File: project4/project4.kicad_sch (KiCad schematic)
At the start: 22 parts, among them J1 Conn_02x07_Row_Letter_First, J2 Conn_02x07_Row_Letter_First, U1 SST27ST020, U2 SST27ST020, U3 74LS02, U4 74LS670, U5 74LS139, U6 74LS670

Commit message: Modify project4
Signed-off-by: Youngki Park <ykp7409@gmail.com>
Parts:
- removed U3: 74LS02, Package_DIP:DIP-14_W7.62mm_Socket, symbol 74xx:74LS02
- added U7: 74LS32, symbol 74xx:74LS32
- added U8: 74LS00, symbol 74xx:74LS00
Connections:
- net +5V: now also U7.14 (VCC)
- net A13: now also U8.1
- net A15: now also U7.9
- net D0: now also U4.15 (D1); no longer U4.3 (D4)
- net D1: now also U4.1 (D2); no longer U4.2 (D3)
- net D2: now also U4.2 (D3); no longer U4.1 (D2)
- net D3: now also U4.3 (D4); no longer U4.15 (D1)
- net GND: now also U4.11 (~{Er}), U6.11 (~{Er}), U7.7 (GND)
- net MA13: now also R4.2, U4.10 (Q1); no longer R1.2, U4.6 (Q4)
- net MA14: now also R3.2, U4.9 (Q2); no longer R2.2, U4.7 (Q3)
- net MA15: now also R2.2, U4.7 (Q3); no longer R3.2, U4.9 (Q2)
- net MA16: now also R1.2, U4.6 (Q4); no longer R4.2, U4.10 (Q1)
- net /SLTSL: now also U7.2
- net /WR: now also U7.1
- net at U4.12 (~{Ew}), U6.12 (~{Ew}): now also U7.6
- new net: U7.10, U8.3
- new net: U7.4, U7.8
- new net: U7.3, U7.5
- new net A14: U8.2
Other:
- moved on the sheet: C3, C5, J1, J2, R1, R2, R3, R4, R5, R6, U4, U5A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

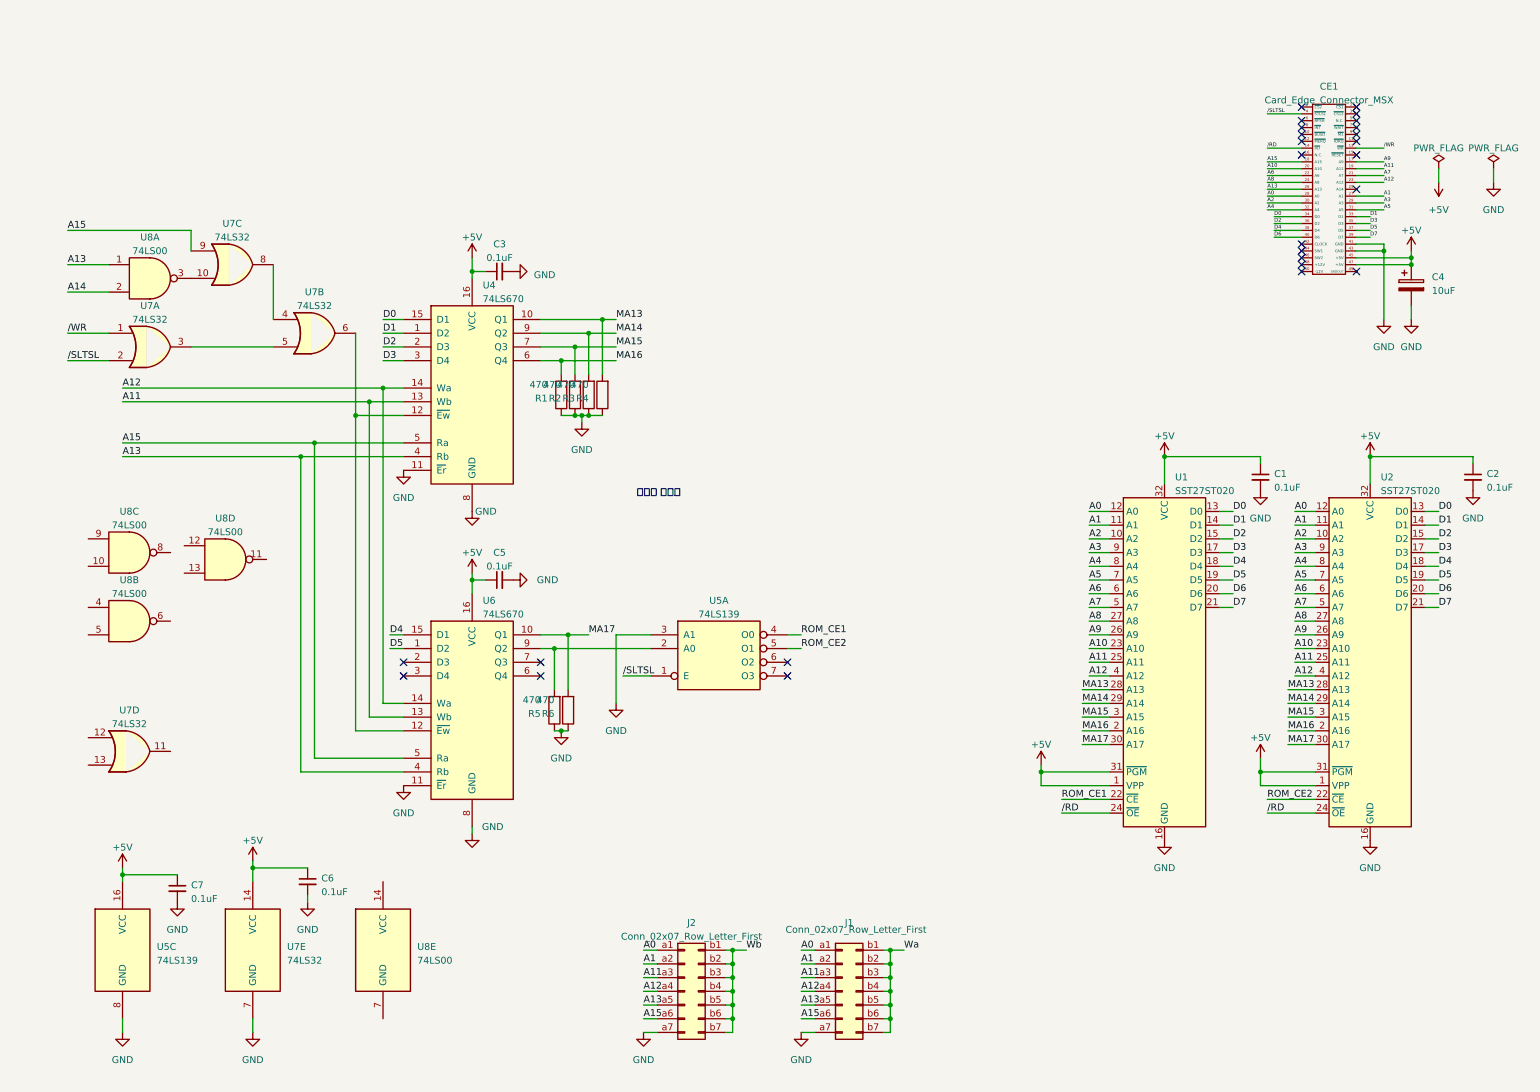
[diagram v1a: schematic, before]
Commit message: Modify PCB4 by ykp74
Signed-off-by: Youngki Park <ykp7409@gmail.com>
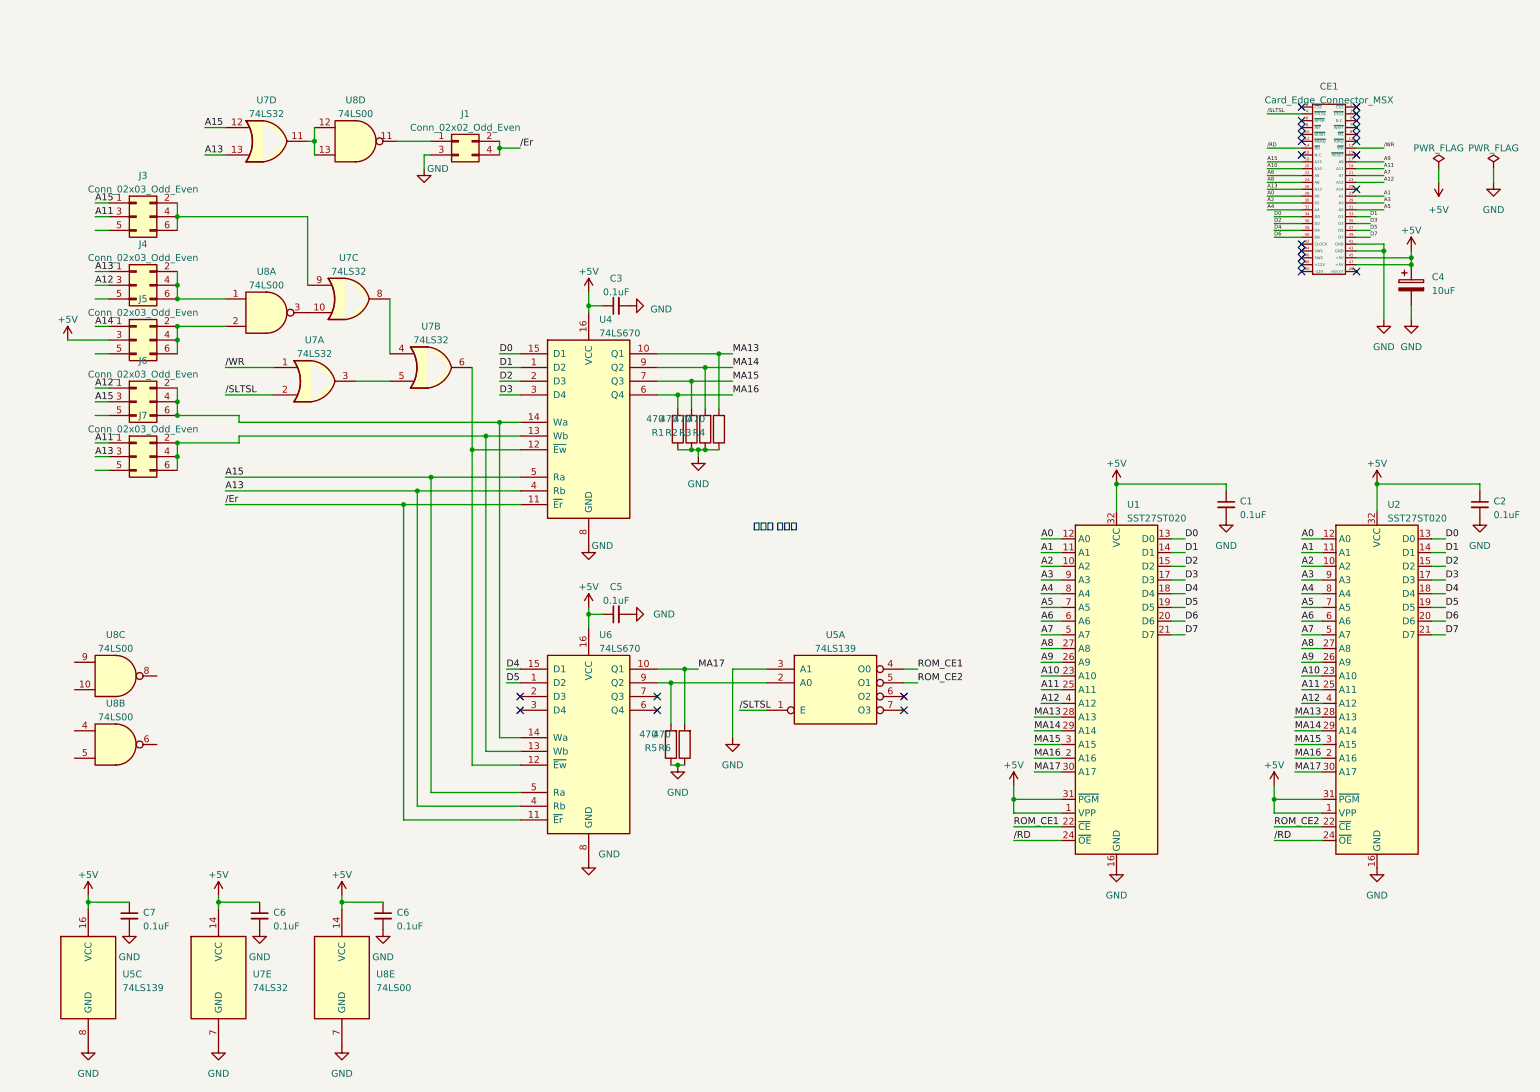
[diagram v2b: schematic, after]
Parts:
- removed J1, J2: Conn_02x07_Row_Letter_First, Connector_PinHeader_2.54mm:PinHeader_2x07_P2.54mm_Vertical, symbol Connector_Generic:Conn_02x07_Row_Letter_First
- added C6: 0.1uF, Capacitor_THT:C_Disc_D6.0mm_W2.5mm_P5.00mm, symbol Device:C_Small
- added J1: Conn_02x02_Odd_Even, symbol Connector_Generic:Conn_02x02_Odd_Even
- added J3, J4, J5, J6, J7: Conn_02x03_Odd_Even, Connector_PinHeader_2.54mm:PinHeader_2x03_P2.54mm_Vertical, symbol Connector_Generic:Conn_02x03_Odd_Even
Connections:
- net +5V: now also U8.14 (VCC), C6.1, J5.3 (Pin_3)
- net A11: now also J3.3 (Pin_3), J7.1 (Pin_1); no longer U4.13 (Wb), U6.13 (Wb)
- net A12: now also J4.3 (Pin_3), J6.1 (Pin_1); no longer U4.14 (Wa), U6.14 (Wa)
- net A13: now also U7.13, J4.1 (Pin_1), J7.3 (Pin_3); no longer U8.1
- net A14: now also J5.1 (Pin_1); no longer U8.2
- net A15: now also U7.12, J3.1 (Pin_1), J6.3 (Pin_3); no longer U7.9
- net GND: now also U8.7 (GND), C6.2, J1.3 (Pin_3); no longer U4.11 (~{Er}), U6.11 (~{Er})
- net at U7.11: now also U8.12, U8.13
- net at U8.11: now also J1.1 (Pin_1)
- new net: J3.2 (Pin_2), J3.4 (Pin_4), J3.6 (Pin_6), U7.9
- new net: J6.2 (Pin_2), J6.4 (Pin_4), J6.6 (Pin_6), U4.14 (Wa), U6.14 (Wa)
- new net: J4.2 (Pin_2), J4.4 (Pin_4), J4.6 (Pin_6), U8.1
- new net: J5.2 (Pin_2), J5.4 (Pin_4), J5.6 (Pin_6), U8.2
- new net: J7.2 (Pin_2), J7.4 (Pin_4), J7.6 (Pin_6), U4.13 (Wb), U6.13 (Wb)
- new net /Er: J1.2 (Pin_2), J1.4 (Pin_4), U4.11 (~{Er}), U6.11 (~{Er})
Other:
- title: 4M Mega Rom Card (ASCII 8k type) -> 4M Mega Rom Card (ASCII 8k / Konami 8k type)
- moved on the sheet: C1, C2, C3, C5, C6, C7, R1, R2, R3, R4, R5, R6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

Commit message: Modify PCB4
Signed-off-by: Youngki Park <ykp7409@gmail.com>
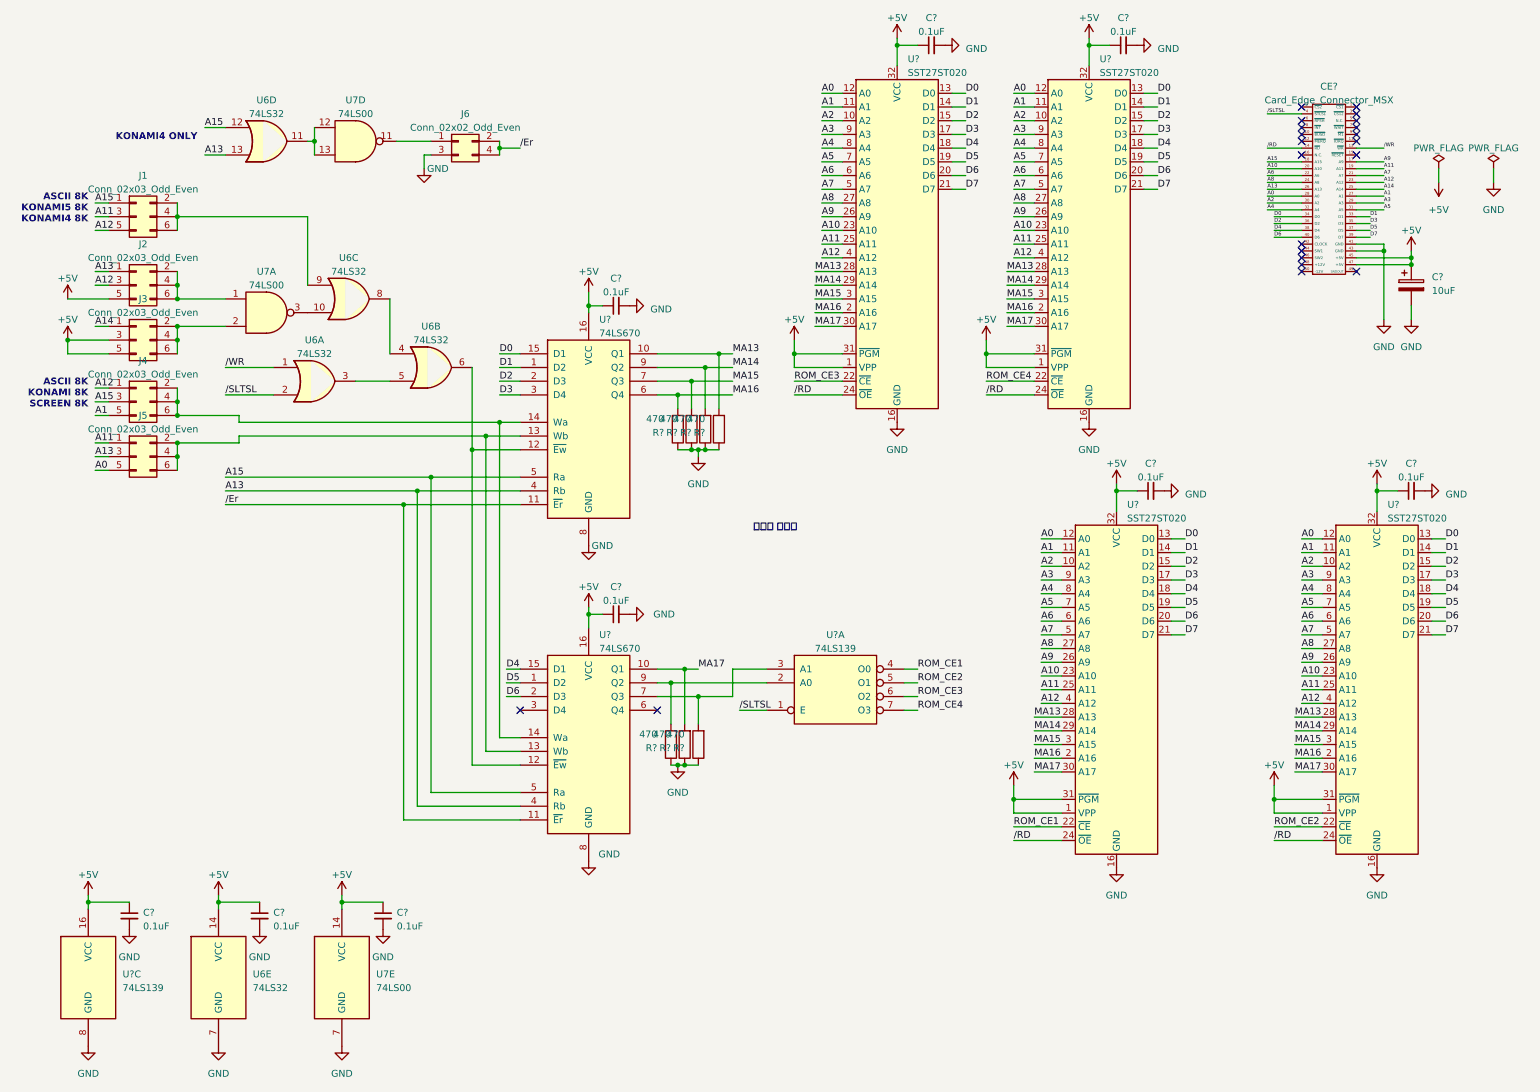
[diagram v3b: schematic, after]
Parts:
- removed unit 3 of U8
- removed unit 2 of U8
- added C? (x2): 0.1uF, Capacitor_THT:C_Disc_D6.0mm_W2.5mm_P5.00mm, symbol Device:C_Small
- added R?: 470, Resistor_THT:R_Axial_DIN0207_L6.3mm_D2.5mm_P10.16mm_Horizontal, symbol Device:R
- added U? (x2): SST27ST020, Package_DIP:DIP-32_W15.24mm_Socket, symbol Memory_Flash_Custom:SST27ST020
- J6: renamed from J1; footprint (none) -> Connector_PinHeader_2.54mm:PinHeader_2x02_P2.54mm_Vertical
- U6: renamed from U7; footprint (none) -> Package_DIP:DIP-14_W7.62mm_Socket
- U7: renamed from U8; footprint (none) -> Package_DIP:DIP-14_W7.62mm_Socket
- renumbered C3 to C?, C7 to C?, C6 to C?, C1 to C?, C4 to C?, C2 to C?, C5 to C?, CE1 to CE?, J3 to J1, J4 to J2, J5 to J3, J6 to J4, J7 to J5, R6 to R?, R4 to R?, R5 to R?, R1 to R?, R3 to R?, R2 to R?, U1 to U?, U2 to U?, U4 to U?, U5 to U?, U6 to U?
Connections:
- net +5V: now also J2.5 (Pin_5), J3.5 (Pin_5), C?.1, C?.1, U?.1 (VPP), U?.1 (VPP), U?.31 (~{PGM}), U?.31 (~{PGM}), U?.32 (VCC), U?.32 (VCC)
- net A0: now also J5.5 (Pin_5), U?.12 (A0), U?.12 (A0)
- net A1: now also J4.5 (Pin_5), U?.11 (A1), U?.11 (A1)
- net A10: now also U?.23 (A10), U?.23 (A10)
- net A11: now also U?.25 (A11), U?.25 (A11)
- net A12: now also J1.5 (Pin_5), U?.4 (A12), U?.4 (A12)
- net A14: now also CE?.25 (A14)
- net A2: now also U?.10 (A2), U?.10 (A2)
- net A3: now also U?.9 (A3), U?.9 (A3)
- net A4: now also U?.8 (A4), U?.8 (A4)
- net A5: now also U?.7 (A5), U?.7 (A5)
- net A6: now also U?.6 (A6), U?.6 (A6)
- net A7: now also U?.5 (A7), U?.5 (A7)
- net A8: now also U?.27 (A8), U?.27 (A8)
- net A9: now also U?.26 (A9), U?.26 (A9)
- net D0: now also U?.13 (D0), U?.13 (D0)
- net D1: now also U?.14 (D1), U?.14 (D1)
- net D2: now also U?.15 (D2), U?.15 (D2)
- net D3: now also U?.17 (D3), U?.17 (D3)
- net D4: now also U?.18 (D4), U?.18 (D4)
- net D5: now also U?.19 (D5), U?.19 (D5)
- net D6: now also U?.2 (D3), U?.20 (D6), U?.20 (D6)
- net D7: now also U?.21 (D7), U?.21 (D7)
- net GND: now also C?.2, C?.2, R?.1, U?.16 (GND), U?.16 (GND); no longer U?.3 (A1)
- net MA13: now also U?.28 (A13), U?.28 (A13)
- net MA14: now also U?.29 (A14), U?.29 (A14)
- net MA15: now also U?.3 (A15), U?.3 (A15)
- net MA16: now also U?.2 (A16), U?.2 (A16)
- net MA17: now also U?.30 (A17), U?.30 (A17)
- net /RD: now also U?.24 (~{OE}), U?.24 (~{OE})
- net ROM_CE3: now reaches U?.6 (O2)
- net ROM_CE3: now also U?.22 (~{CE})
- net ROM_CE4: now reaches U?.7 (O3)
- net ROM_CE4: now also U?.22 (~{CE})
- net at U?.7 (Q3): now also U?.3 (A1), R?.2
- no-connect marks 26 -> 21
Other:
- note added: "ASCII 8K KONAMI 8K SCREEN 8K"
- note added: "ASCII 8K KONAMI5 8K KONAMI4 8K"
- note added: "KONAMI4 ONLY"
- moved on the sheet: C?

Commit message: Modified PCB 4
Signed-off-by: ykp74 <ykp7409@gmail.com>
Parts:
- J1, J2, J3, J4, J5: value Conn_02x03_Odd_Even -> Conn_02x03
- J6: value Conn_02x02_Odd_Even -> Conn_02x02
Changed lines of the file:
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@@
       (effects (font (size 1.27 1.27)))
     )
-    (property "Value" "Conn_02x02_Odd_Even" (at 88.9 21.59 0)
+    (property "Value" "Conn_02x02" (at 88.9 21.59 0)
       (effects (font (size 1.27 1.27)))
     )
@@
       (effects (font (size 1.27 1.27)))
     )
-    (property "Value" "Conn_02x03_Odd_Even" (at 29.21 67.31 0)
+    (property "Value" "Conn_02x03" (at 29.21 67.31 0)
       (effects (font (size 1.27 1.27)))
     )
@@
       (effects (font (size 1.27 1.27)))
     )
-    (property "Value" "Conn_02x03_Odd_Even" (at 29.21 55.88 0)
+    (property "Value" "Conn_02x03" (at 29.21 55.88 0)
       (effects (font (size 1.27 1.27)))
     )
@@
       (effects (font (size 1.27 1.27)))
     )
-    (property "Value" "Conn_02x03_Odd_Even" (at 29.21 77.47 0)
+    (property "Value" "Conn_02x03" (at 29.21 77.47 0)
       (effects (font (size 1.27 1.27)))
     )
@@
       (effects (font (size 1.27 1.27)))
     )
-    (property "Value" "Conn_02x03_Odd_Even" (at 29.21 33.02 0)
+    (property "Value" "Conn_02x03" (at 29.21 33.02 0)
       (effects (font (size 1.27 1.27)))
     )
@@
       (effects (font (size 1.27 1.27)))
     )
-    (property "Value" "Conn_02x03_Odd_Even" (at 29.21 45.72 0)
-      (effects (font (size 1.27 1.27)))
-    )
+    (property "Value" "Conn_02x03" (at 29.21 45.72 0)
+      (effects (font (size 1.27 1.27)))
+    )

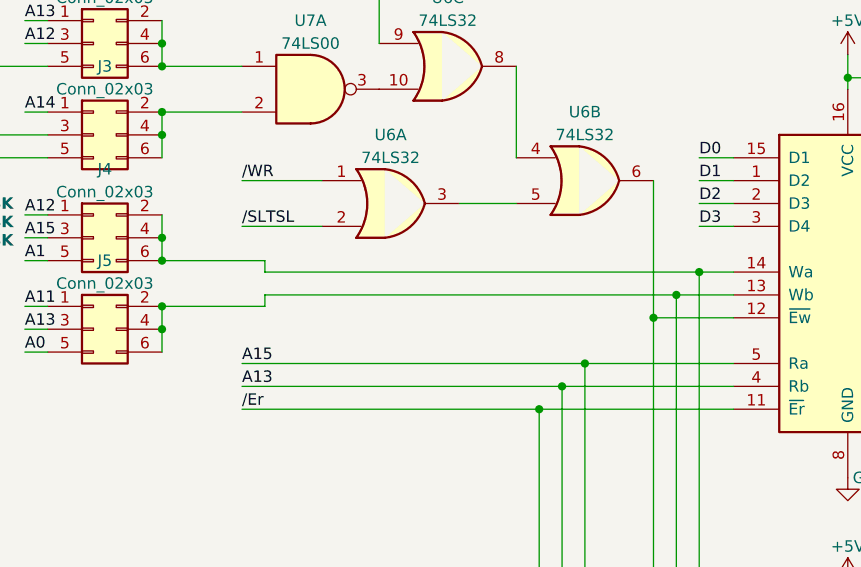
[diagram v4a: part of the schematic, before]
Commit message: Modify PCB4
Signed-off-by: Youngki Park <ykp7409@gmail.com>
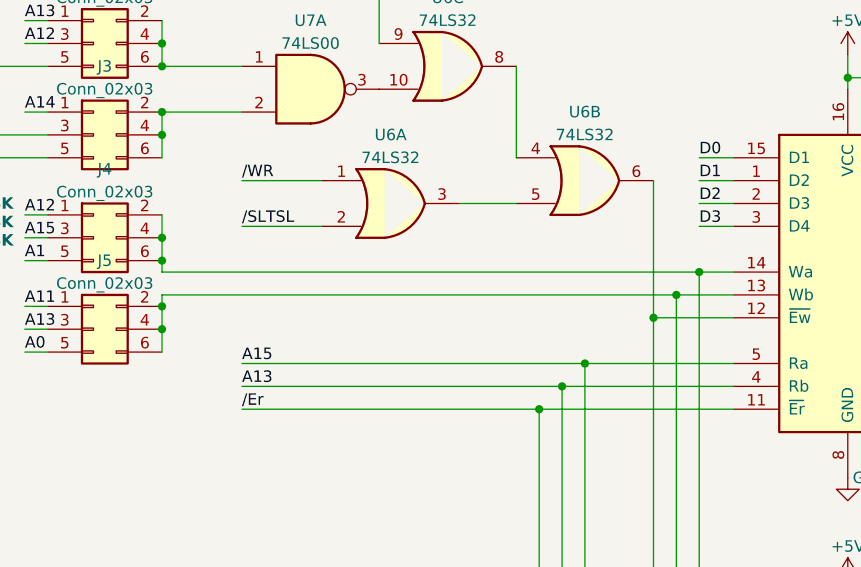
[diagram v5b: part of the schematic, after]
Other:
- title: 4M Mega Rom Card (ASCII 8k / Konami 8k type) -> 8M Mega Rom Card (ASCII 8k / Konami 8k type)
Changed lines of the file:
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@@
   (paper "A4")
   (title_block
-    (title "4M Mega Rom Card (ASCII 8k / Konami 8k type)")
+    (title "8M Mega Rom Card (ASCII 8k / Konami 8k type)")
     (date "2023-04-13")
     (rev "1.5")
@@
     (stroke (width 0) (type default))
   )
-  (wire (pts (xy 46.99 80.01) (xy 46.99 78.74))
-    (stroke (width 0) (type default))
-  )
   (wire (pts (xy 279.4 29.21) (xy 279.4 31.75))
     (stroke (width 0) (type default))
@@
     (stroke (width 0) (type default))
   )
-  (wire (pts (xy 46.99 74.93) (xy 46.99 76.2))
-    (stroke (width 0) (type default))
-  )
   (wire (pts (xy 111.76 111.76) (xy 111.76 114.3))
     (stroke (width 0) (type default))
@@
     (stroke (width 0) (type default))
   )
-  (wire (pts (xy 46.99 78.74) (xy 92.71 78.74))
-    (stroke (width 0) (type default))
-  )
   (wire (pts (xy 158.75 66.04) (xy 149.86 66.04))
     (stroke (width 0) (type default))
@@
     (stroke (width 0) (type default))
   )
-  (wire (pts (xy 35.56 74.93) (xy 46.99 74.93))
+  (wire (pts (xy 35.56 76.2) (xy 95.25 76.2))
     (stroke (width 0) (type default))
   )
@@
     (stroke (width 0) (type default))
   )
+  (wire (pts (xy 35.56 76.2) (xy 35.56 74.93))
+    (stroke (width 0) (type default))
+  )
   (wire (pts (xy 40.64 21.59) (xy 44.45 21.59))
     (stroke (width 0) (type default))
@@
     (stroke (width 0) (type default))
   )
-  (wire (pts (xy 46.99 76.2) (xy 95.25 76.2))
-    (stroke (width 0) (type default))
-  )
   (wire (pts (xy 20.32 80.01) (xy 22.86 80.01))
     (stroke (width 0) (type default))
@@
     (stroke (width 0) (type default))
   )
+  (wire (pts (xy 35.56 78.74) (xy 35.56 80.01))
+    (stroke (width 0) (type default))
+  )
   (wire (pts (xy 96.52 127) (xy 99.06 127))
     (stroke (width 0) (type default))
@@
     (stroke (width 0) (type default))
   )
-  (wire (pts (xy 35.56 80.01) (xy 46.99 80.01))
-    (stroke (width 0) (type default))
-  )
+  (wire (pts (xy 35.56 78.74) (xy 92.71 78.74))
+    (stroke (width 0) (type default))
+  )
